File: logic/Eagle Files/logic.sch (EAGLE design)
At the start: 65 parts, among them J2 B2PS-VH(LF)(SN), J3 B2PS-VH(LF)(SN), J4 B2PS-VH(LF)(SN), J6 B2PS-VH(LF)(SN), Q4 STT4P3LLH6, T1 R-78E5.0-1.0, U1 9DoF IMU, U4 TLV70233DBVR, X1 MINI-USB_SHIELD5P4-32005-400, X2 C-GRID-05-15-91, X5 C-GRID-05-15-91, X7 SI-50170

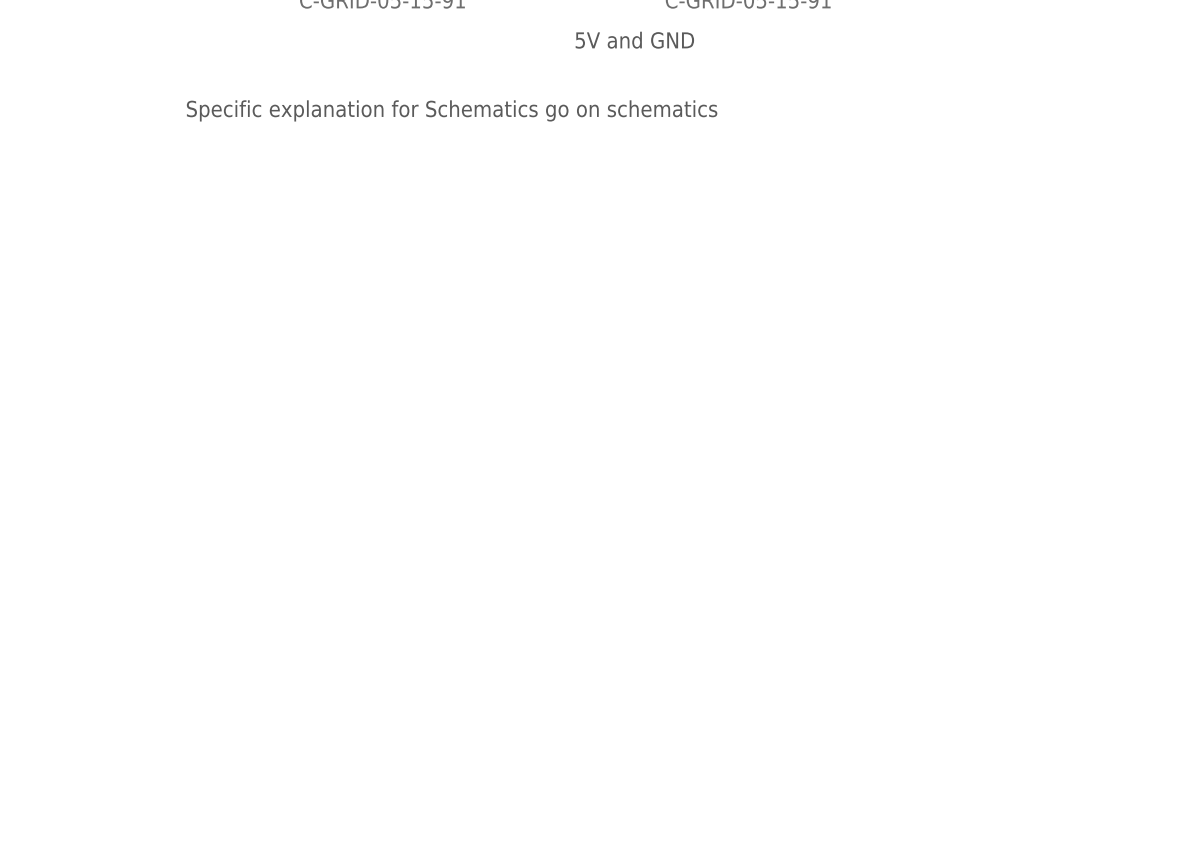
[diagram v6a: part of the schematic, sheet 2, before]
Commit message: added IMA198 to sch
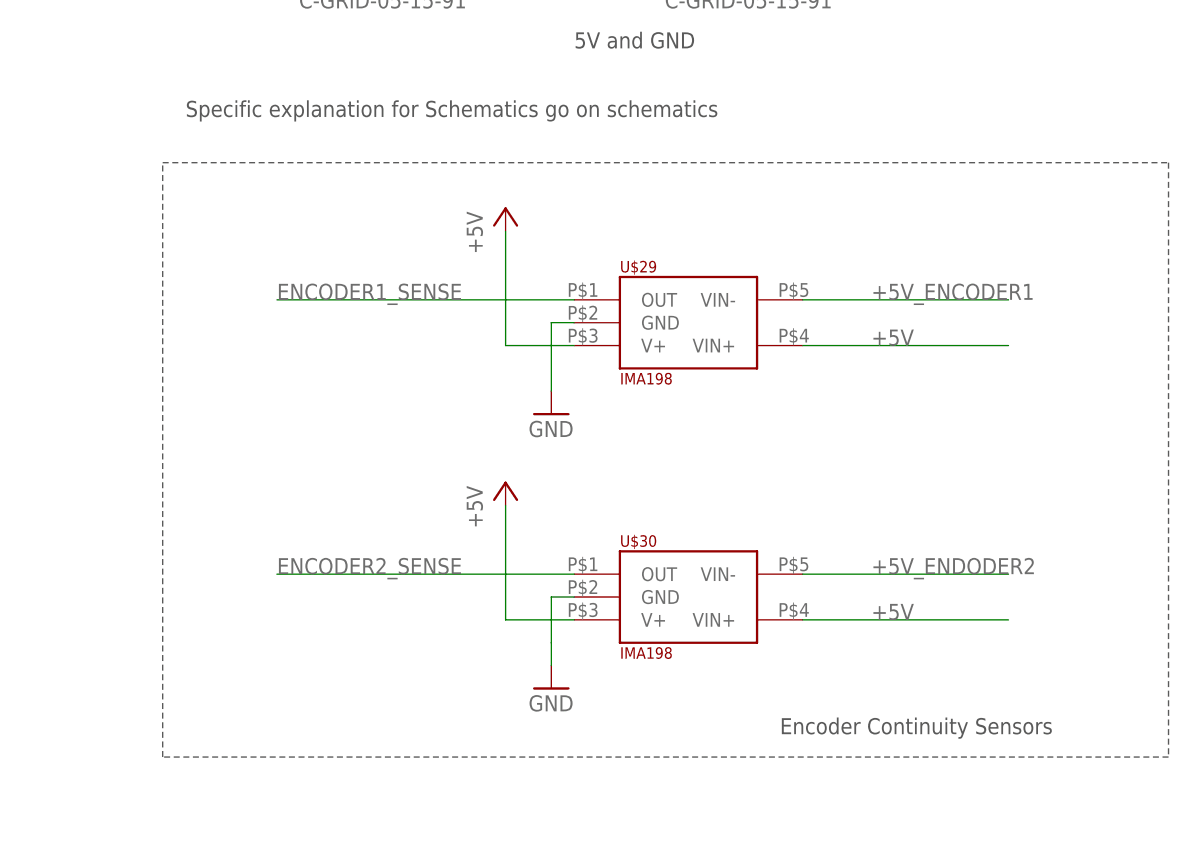
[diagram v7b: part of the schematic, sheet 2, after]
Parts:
- added U$29, U$30: IMA198, IGVC-Sensor:IMA198
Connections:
- new net +5V_ENCODER1: U$29.VIN-
- new net +5V_ENDODER2: U$30.VIN-
- new net ENCODER1_SENSE: U$29.OUT
- new net ENCODER2_SENSE: U$30.OUT
- net +5V: now also U$29.V+, U$29.VIN+, U$30.V+, U$30.VIN+
- net GND: now also U$29.GND, U$30.GND
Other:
- note added: "Encoder Continuity Sensors"
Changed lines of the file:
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@@
 <?xml version="1.0" encoding="utf-8"?>
 <!DOCTYPE eagle SYSTEM "eagle.dtd">
-<eagle version="9.2.0">
+<eagle version="9.1.1">
 <drawing>
 <settings>
@@
 <part name="U$28" library="IGVC-Discrete" deviceset="S10M-TP" device=""/>
 <part name="P+20" library="supply1" library_urn="urn:adsk.eagle:library:371" deviceset="+24V" device=""/>
+<part name="U$29" library="IGVC-Sensor" deviceset="IMA198" device=""/>
+<part name="U$30" library="IGVC-Sensor" deviceset="IMA198" device=""/>
+<part name="GND13" library="supply1" library_urn="urn:adsk.eagle:library:371" deviceset="GND" device=""/>
+<part name="P+5" library="supply1" library_urn="urn:adsk.eagle:library:371" deviceset="+5V" device=""/>
+<part name="P+7" library="supply1" library_urn="urn:adsk.eagle:library:371" deviceset="+5V" device=""/>
+<part name="GND14" library="supply1" library_urn="urn:adsk.eagle:library:371" deviceset="GND" device=""/>
 </parts>
 <sheets>
@@
 <text x="64.77" y="81.28" size="2.54" layer="103" font="vector">Sawtooth Motor Controller</text>
 <text x="64.77" y="96.52" size="1.27" layer="103">add level shifter for motor control</text>
+<wire x1="160.02" y1="162.56" x2="271.78" y2="162.56" width="0.1524" layer="97" style="shortdash"/>
+<wire x1="271.78" y1="162.56" x2="271.78" y2="96.52" width="0.1524" layer="97" style="shortdash"/>
+<wire x1="271.78" y1="96.52" x2="160.02" y2="96.52" width="0.1524" layer="97" style="shortdash"/>
+<wire x1="160.02" y1="96.52" x2="160.02" y2="162.56" width="0.1524" layer="97" style="shortdash"/>
+<text x="228.6" y="99.06" size="1.778" layer="97" font="vector">Encoder Continuity Sensors</text>
 </plain>
 <instances>
@@
 <attribute name="VALUE" x="35.56" y="88.9" size="1.778" layer="96"/>
 </instance>
+<instance part="U$29" gate="G$1" x="210.82" y="139.7"/>
+<instance part="U$30" gate="G$1" x="210.82" y="109.22"/>
+<instance part="GND13" gate="1" x="203.2" y="134.62"/>
+<instance part="P+5" gate="1" x="198.12" y="157.48"/>
+<instance part="P+7" gate="1" x="198.12" y="127"/>
+<instance part="GND14" gate="1" x="203.2" y="104.14"/>
 </instances>
 <busses>
@@
 <wire x1="38.1" y1="97.79" x2="43.18" y2="97.79" width="0.1524" layer="91"/>
 </segment>
+<segment>
+<pinref part="U$29" gate="G$1" pin="GND"/>
+<pinref part="GND13" gate="1" pin="GND"/>
+<wire x1="205.74" y1="144.78" x2="203.2" y2="144.78" width="0.1524" layer="91"/>
+<wire x1="203.2" y1="144.78" x2="203.2" y2="137.16" width="0.1524" layer="91"/>
+</segment>
+<segment>
+<pinref part="U$30" gate="G$1" pin="GND"/>
+<wire x1="205.74" y1="114.3" x2="203.2" y2="114.3" width="0.1524" layer="91"/>
+<wire x1="203.2" y1="114.3" x2="203.2" y2="109.22" width="0.1524" layer="91"/>
+<pinref part="GND14" gate="1" pin="GND"/>
+<wire x1="203.2" y1="109.22" x2="203.2" y2="106.68" width="0.1524" layer="91"/>
+</segment>
 </net>
 <net name="+3V3" class="0">
@@
 <label x="243.84" y="190.5" size="1.27" layer="95" xref="yes"/>
 </segment>
+<segment>
+<pinref part="U$29" gate="G$1" pin="V+"/>
+<pinref part="P+5" gate="1" pin="+5V"/>
+<wire x1="205.74" y1="142.24" x2="198.12" y2="142.24" width="0.1524" layer="91"/>
+<wire x1="198.12" y1="142.24" x2="198.12" y2="154.94" width="0.1524" layer="91"/>
+</segment>
+<segment>
+<pinref part="U$30" gate="G$1" pin="V+"/>
+<pinref part="P+7" gate="1" pin="+5V"/>
+<wire x1="205.74" y1="111.76" x2="198.12" y2="111.76" width="0.1524" layer="91"/>
+<wire x1="198.12" y1="111.76" x2="198.12" y2="124.46" width="0.1524" layer="91"/>
+</segment>
+<segment>
+<pinref part="U$29" gate="G$1" pin="VIN+"/>
+<wire x1="231.14" y1="142.24" x2="254" y2="142.24" width="0.1524" layer="91"/>
+<label x="238.76" y="142.24" size="1.778" layer="95"/>
+</segment>
+<segment>
+<pinref part="U$30" gate="G$1" pin="VIN+"/>
+<wire x1="231.14" y1="111.76" x2="254" y2="111.76" width="0.1524" layer="91"/>
+<label x="238.76" y="111.76" size="1.778" layer="95"/>
+</segment>
 </net>
 <net name="MOTOR_CTRL" class="0">
@@
 </segment>
 </net>
+<net name="ENCODER1_SENSE" class="0">
+<segment>
+<pinref part="U$29" gate="G$1" pin="OUT"/>
+<wire x1="205.74" y1="147.32" x2="172.72" y2="147.32" width="0.1524" layer="91"/>
+<label x="172.72" y="147.32" size="1.778" layer="95"/>
+</segment>
+</net>
+<net name="ENCODER2_SENSE" class="0">
+<segment>
+<pinref part="U$30" gate="G$1" pin="OUT"/>
+<wire x1="205.74" y1="116.84" x2="172.72" y2="116.84" width="0.1524" layer="91"/>
+<label x="172.72" y="116.84" size="1.778" layer="95"/>
+</segment>
+</net>
+<net name="+5V_ENCODER1" class="0">
+<segment>
+<pinref part="U$29" gate="G$1" pin="VIN-"/>
+<wire x1="231.14" y1="147.32" x2="254" y2="147.32" width="0.1524" layer="91"/>
+<label x="238.76" y="147.32" size="1.778" layer="95"/>
+</segment>
+</net>
+<net name="+5V_ENDODER2" class="0">
+<segment>
+<pinref part="U$30" gate="G$1" pin="VIN-"/>
+<wire x1="231.14" y1="116.84" x2="254" y2="116.84" width="0.1524" layer="91"/>
+<label x="238.76" y="116.84" size="1.778" layer="95"/>
+</segment>
+</net>

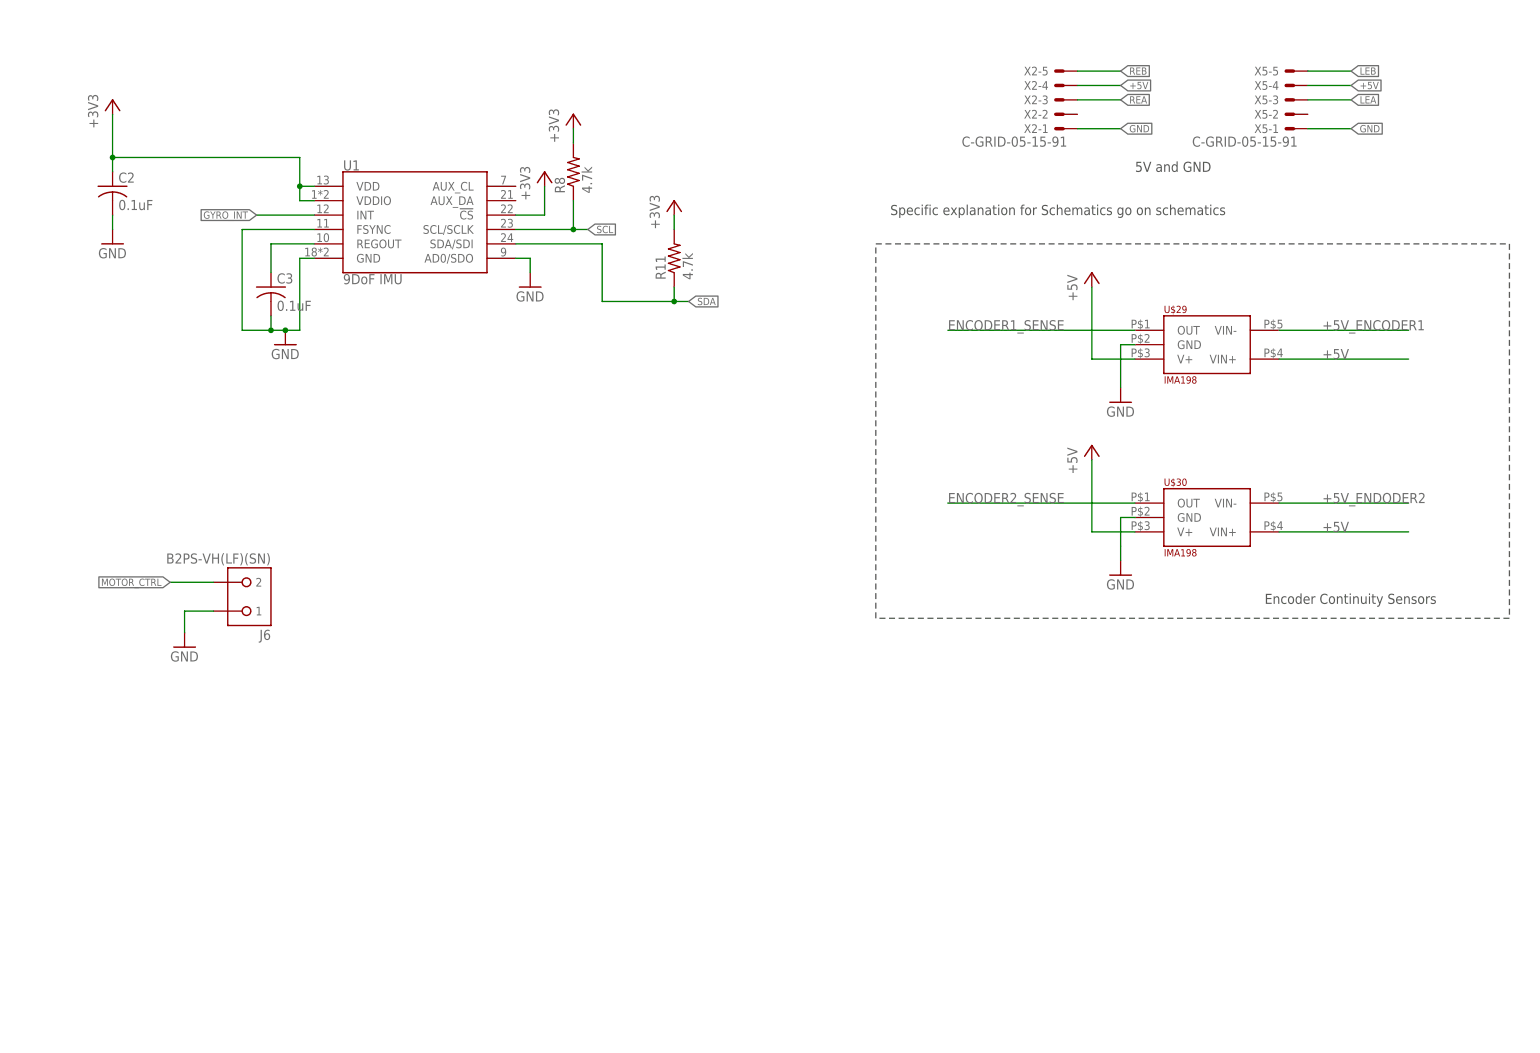
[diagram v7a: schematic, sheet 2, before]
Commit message: removed IMU from sch
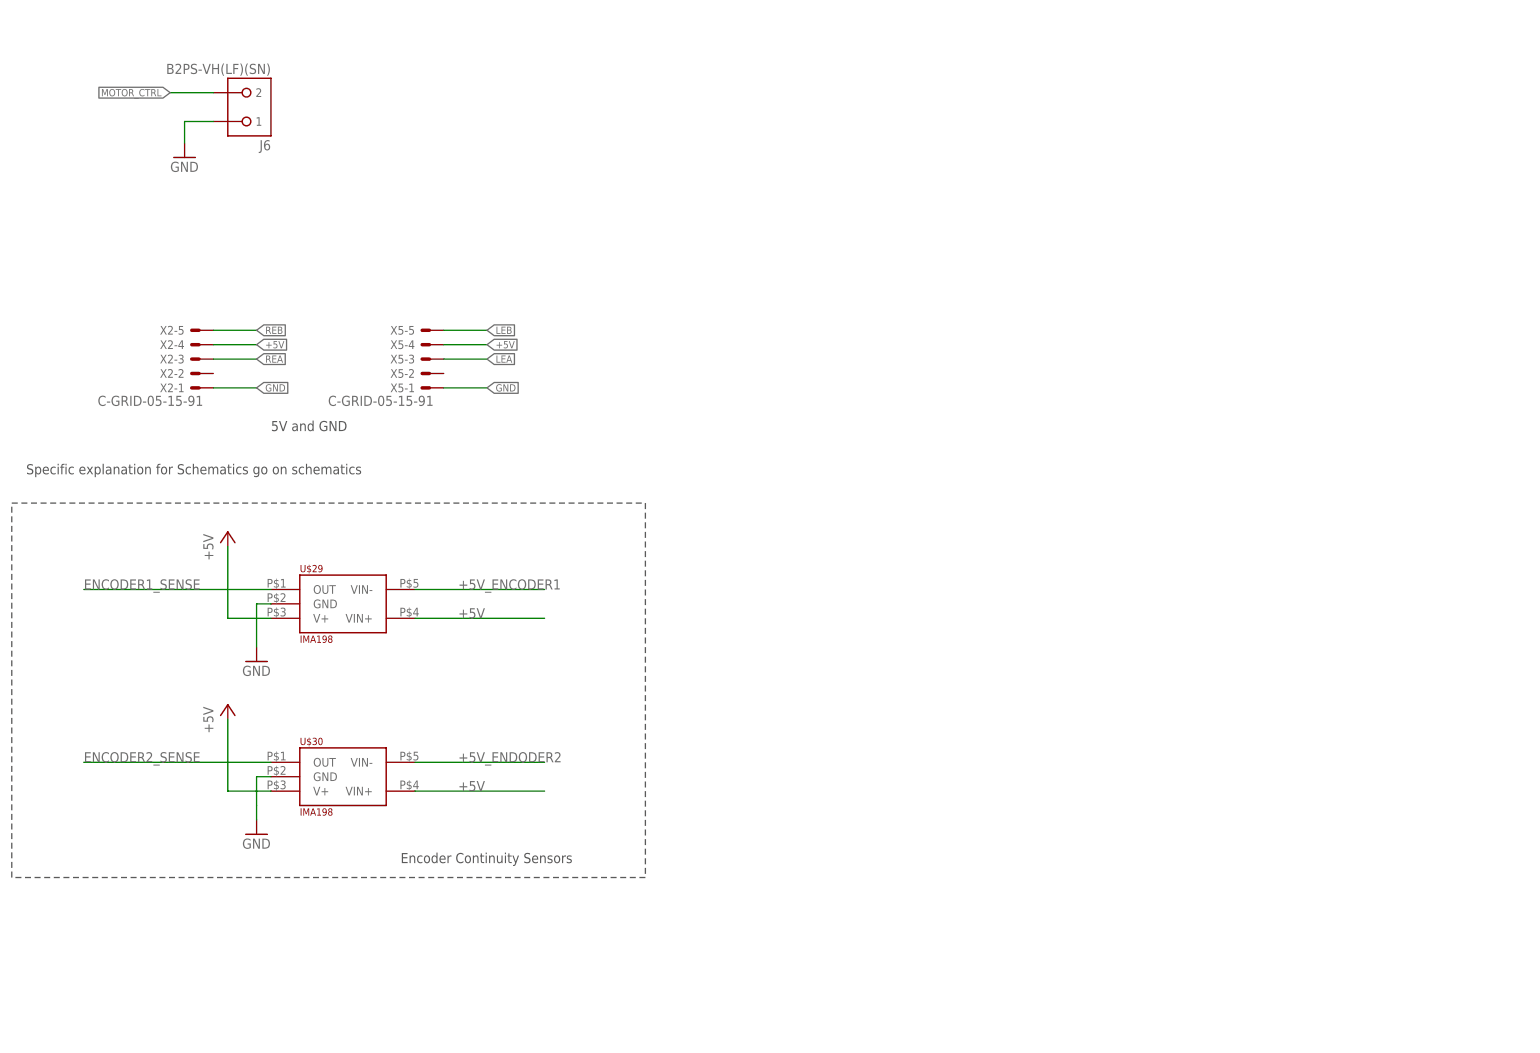
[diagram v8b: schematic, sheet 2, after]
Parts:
- removed C2, C3: 0.1uF, rcl:C-USC0603
- removed R11, R8: 4.7k, rcl:R-US_R0603
- removed U1: 9DoF IMU, SparkFun-Sensors:MPU-9250
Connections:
- removed net GYRO_INT: U1.INT
- removed net REGOUT_C: C3.1, U1.REGOUT
- net +3V3: no longer C2.1, R11.2, R8.2, U1.!CS, U1.VDD, U1.VDDIO
- net GND: no longer C2.2, C3.2, U1.AD0/SDO, U1.FSYNC, U1.GND
- net SCL: no longer R8.1, U1.SCL/SCLK
- net SDA: no longer R11.1, U1.SDA/SDI
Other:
- note added: "Wireless Connector: - ENCODER1_SENSE - ENCODER2_SENSE"
- note removed: "IMU"
- moved on the sheet: J6, U$29, U$30, X2-1, X2-2, X2-3, X2-4, X2-5, X5-1, X5-2, X5-3, X5-4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
